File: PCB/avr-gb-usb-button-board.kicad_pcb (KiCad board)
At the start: 2 copper layers, 81 x 48 mm, 13 parts, among them IC1 ATTINY88-A

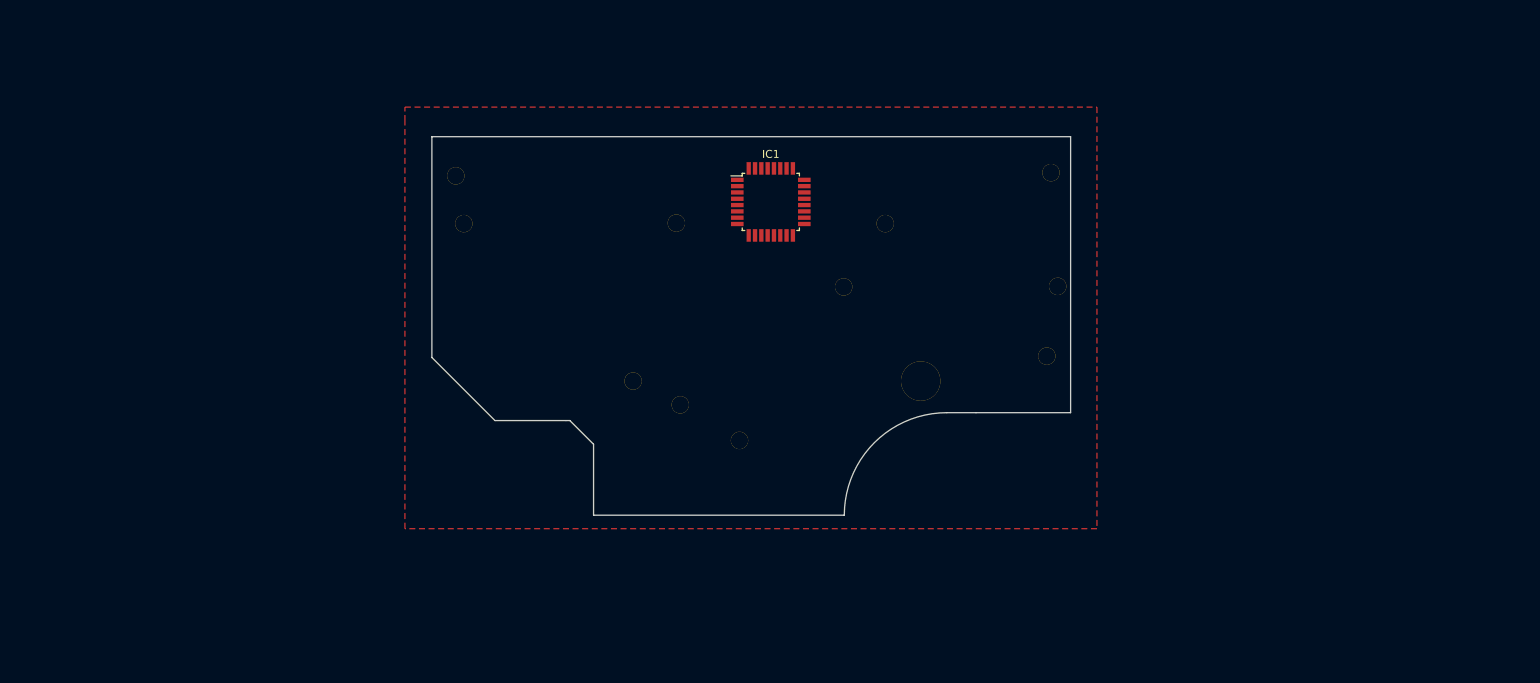
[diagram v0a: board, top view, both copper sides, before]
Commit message: Added mounting holes
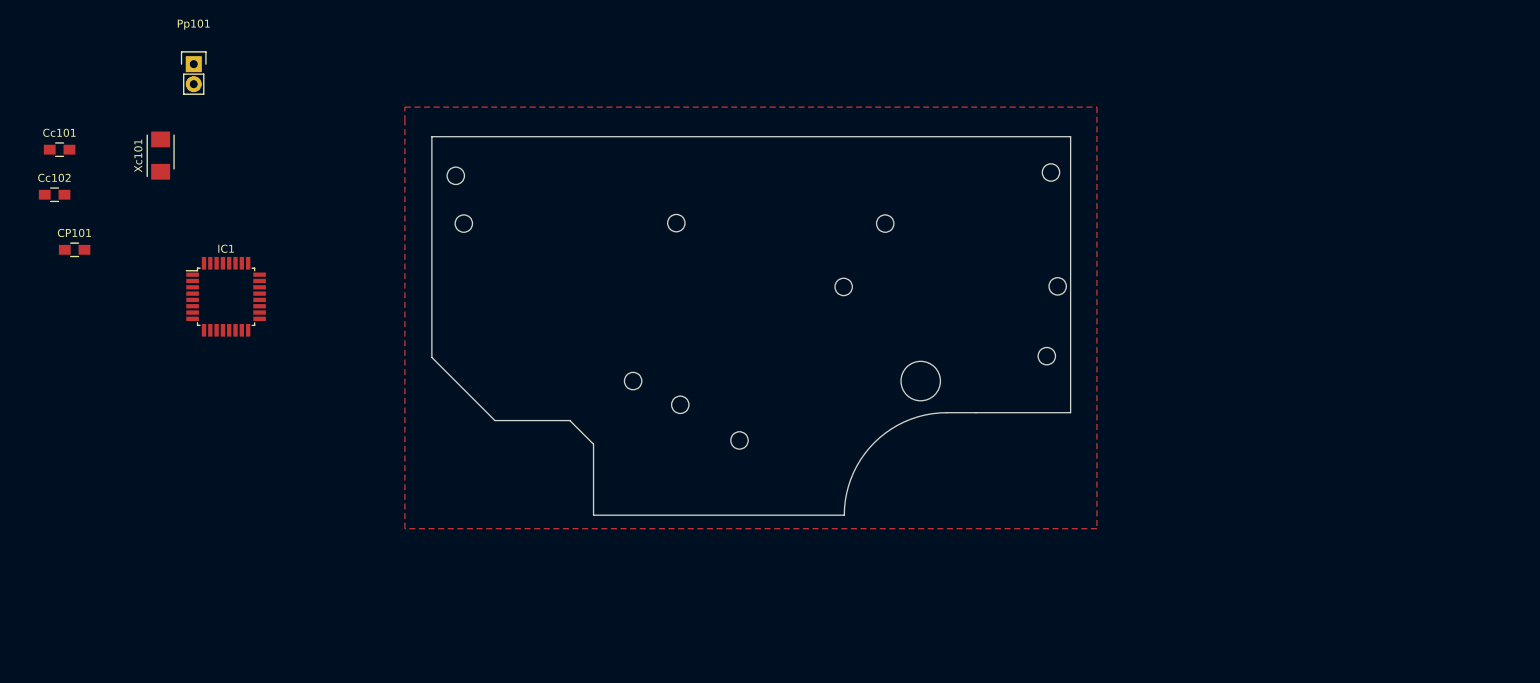
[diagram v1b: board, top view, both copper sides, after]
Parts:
- removed the ? at (44.9, 52.2)
- removed the ? at (50.4, 32.2)
- removed the ? at (23.4, 32.2)
- removed the ? at (22.4, 26.2)
- removed the ? at (50.9, 55.2)
- removed the ? at (58.4, 59.7)
- removed the ? at (81.4, 52.2)
- removed the ? at (97.4, 49.0)
- removed the ? at (98.8, 40.2)
- removed the ? at (97.9, 25.8)
- removed the ? at (76.9, 32.2)
- removed the ? at (71.6, 40.2)
- added ?: , Mounting_Holes:MountingHole_2.2mm_M2, F.Cu at (22.4, 26.2)
- added ?: , Mounting_Holes:MountingHole_2.2mm_M2, F.Cu at (50.9, 55.2)
- added ?: , Mounting_Holes:MountingHole_2.2mm_M2, F.Cu at (44.9, 52.2)
- added ?: , Mounting_Holes:MountingHole_5mm, F.Cu at (81.4, 52.2)
- added ?: , Mounting_Holes:MountingHole_2.2mm_M2, F.Cu at (23.4, 32.2)
- added ?: , Mounting_Holes:MountingHole_2.2mm_M2, F.Cu at (50.4, 32.2)
- added ?: , Mounting_Holes:MountingHole_2.2mm_M2, F.Cu at (76.9, 32.2)
- added ?: , Mounting_Holes:MountingHole_2.2mm_M2, F.Cu at (71.6, 40.2)
- added ?: , Mounting_Holes:MountingHole_2.2mm_M2, F.Cu at (97.9, 25.7)
- added ?: , Mounting_Holes:MountingHole_2.2mm_M2, F.Cu at (98.8, 40.2)
- added ?: , Mounting_Holes:MountingHole_2.2mm_M2, F.Cu at (97.4, 49.0)
- added ?: , Mounting_Holes:MountingHole_2.2mm_M2, F.Cu at (58.4, 59.7)
- added CP101: C, Capacitors_SMD:C_0805_HandSoldering, F.Cu at (-25.9, 35.5)
- added Cc101: 22pF, Capacitors_SMD:C_0805_HandSoldering, F.Cu at (-27.8, 22.8)
- added Cc102: 22pF, Capacitors_SMD:C_0805_HandSoldering, F.Cu at (-28.4, 28.6)
- added Pp101: CONN_01X02, Pin_Headers:Pin_Header_Straight_1x02, F.Cu at (-10.8, 12.0)
- added Xc101: 12MHz, Crystals:Crystal_SMD_5032_2Pads, F.Cu at (-15.0, 23.6)
- moved IC1 70.1 mm to (-6.70, 41.5)
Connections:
- IC1 pad 1: (no net) -> Net-(IC1-Pad1)
- IC1 pad 10: (no net) -> Net-(IC1-Pad10)
- IC1 pad 11: (no net) -> Net-(IC1-Pad11)
- IC1 pad 12: (no net) -> Net-(IC1-Pad12)
- IC1 pad 13: (no net) -> Net-(IC1-Pad13)
- IC1 pad 14: (no net) -> Net-(IC1-Pad14)
- IC1 pad 15: (no net) -> Net-(IC1-Pad15)
- IC1 pad 16: (no net) -> Net-(IC1-Pad16)
- IC1 pad 17: (no net) -> Net-(Cc101-Pad2)
- IC1 pad 18: (no net) -> Net-(IC1-Pad18)
- IC1 pad 19: (no net) -> Net-(IC1-Pad19)
- IC1 pad 2: (no net) -> Net-(IC1-Pad2)
- IC1 pad 20: (no net) -> Net-(IC1-Pad20)
- IC1 pad 21: (no net) -> Net-(IC1-Pad21)
- IC1 pad 22: (no net) -> Net-(IC1-Pad22)
- IC1 pad 23: (no net) -> Net-(IC1-Pad23)
- IC1 pad 24: (no net) -> Net-(IC1-Pad24)
- IC1 pad 25: (no net) -> Net-(IC1-Pad25)
- IC1 pad 26: (no net) -> Net-(IC1-Pad26)
- IC1 pad 27: (no net) -> Net-(IC1-Pad27)
- IC1 pad 28: (no net) -> Net-(IC1-Pad28)
- IC1 pad 29: (no net) -> Net-(IC1-Pad29)
- IC1 pad 3: (no net) -> Net-(IC1-Pad3)
- IC1 pad 30: (no net) -> Net-(IC1-Pad30)
- IC1 pad 31: (no net) -> Net-(IC1-Pad31)
- IC1 pad 32: (no net) -> Net-(IC1-Pad32)
- IC1 pad 4: (no net) -> VCC
- IC1 pad 6: (no net) -> Net-(IC1-Pad6)
- IC1 pad 7: (no net) -> Net-(Cc102-Pad2)
- IC1 pad 8: (no net) -> Net-(IC1-Pad8)
- IC1 pad 9: (no net) -> Net-(IC1-Pad9)

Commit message: Added ABXY button markers
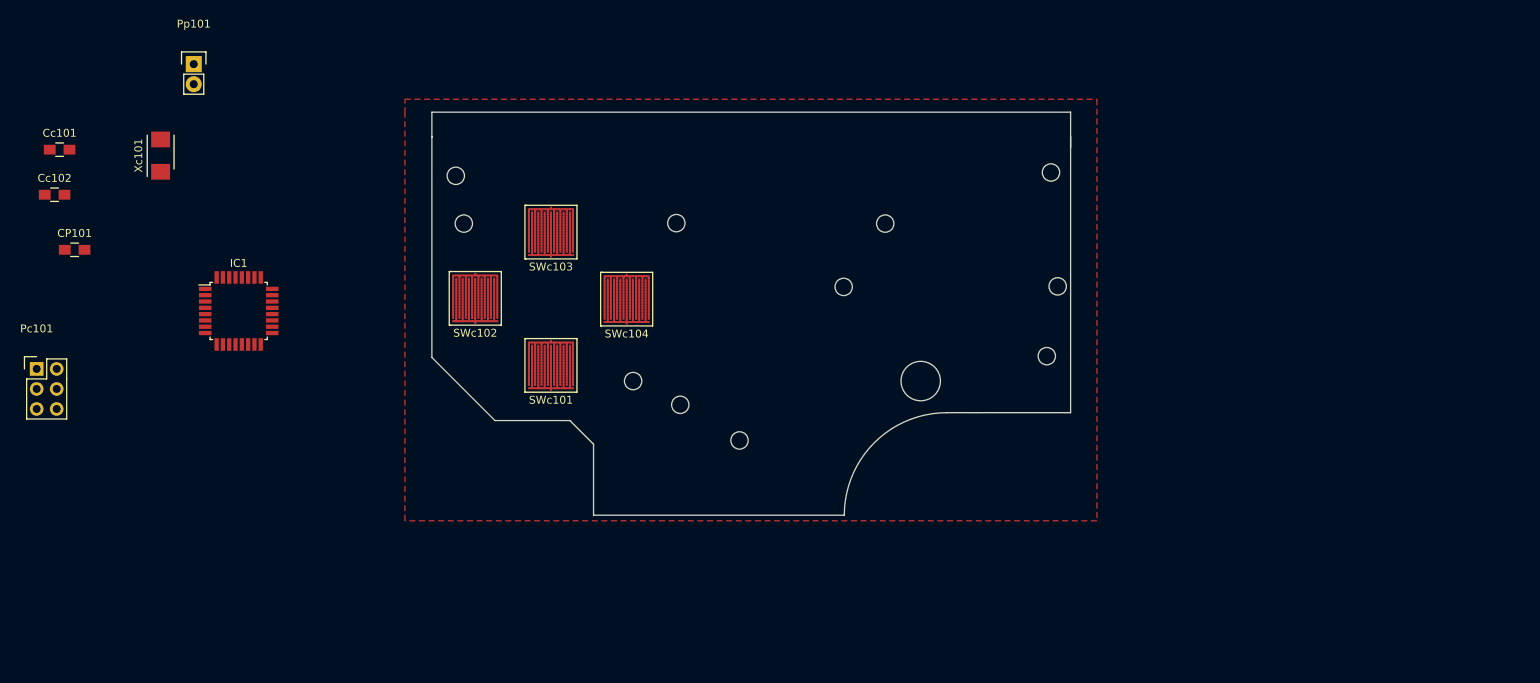
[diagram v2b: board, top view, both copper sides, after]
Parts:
- added Pc101: CONN_02X03, Pin_Headers:Pin_Header_Straight_2x03, F.Cu at (-30.7, 50.6)
- added SWc101: SW_PUSH, GBFootprints:GBButtonPad5mm, F.Cu at (34.5, 49.9)
- added SWc102: SW_PUSH, GBFootprints:GBButtonPad5mm, F.Cu at (24.9, 41.4)
- added SWc103: SW_PUSH, GBFootprints:GBButtonPad5mm, F.Cu at (34.5, 33.0)
- added SWc104: SW_PUSH, GBFootprints:GBButtonPad5mm, F.Cu at (44.1, 41.5)
- moved IC1 2.41 mm to (-5.10, 43.3)
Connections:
- IC1 pad 17: Net-(Cc101-Pad2) -> Net-(IC1-Pad17)
- IC1 pad 7: Net-(Cc102-Pad2) -> Net-(IC1-Pad7)
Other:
- board size 81 x 48 mm -> 81 x 51.1 mm

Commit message: Placed start and select buttons
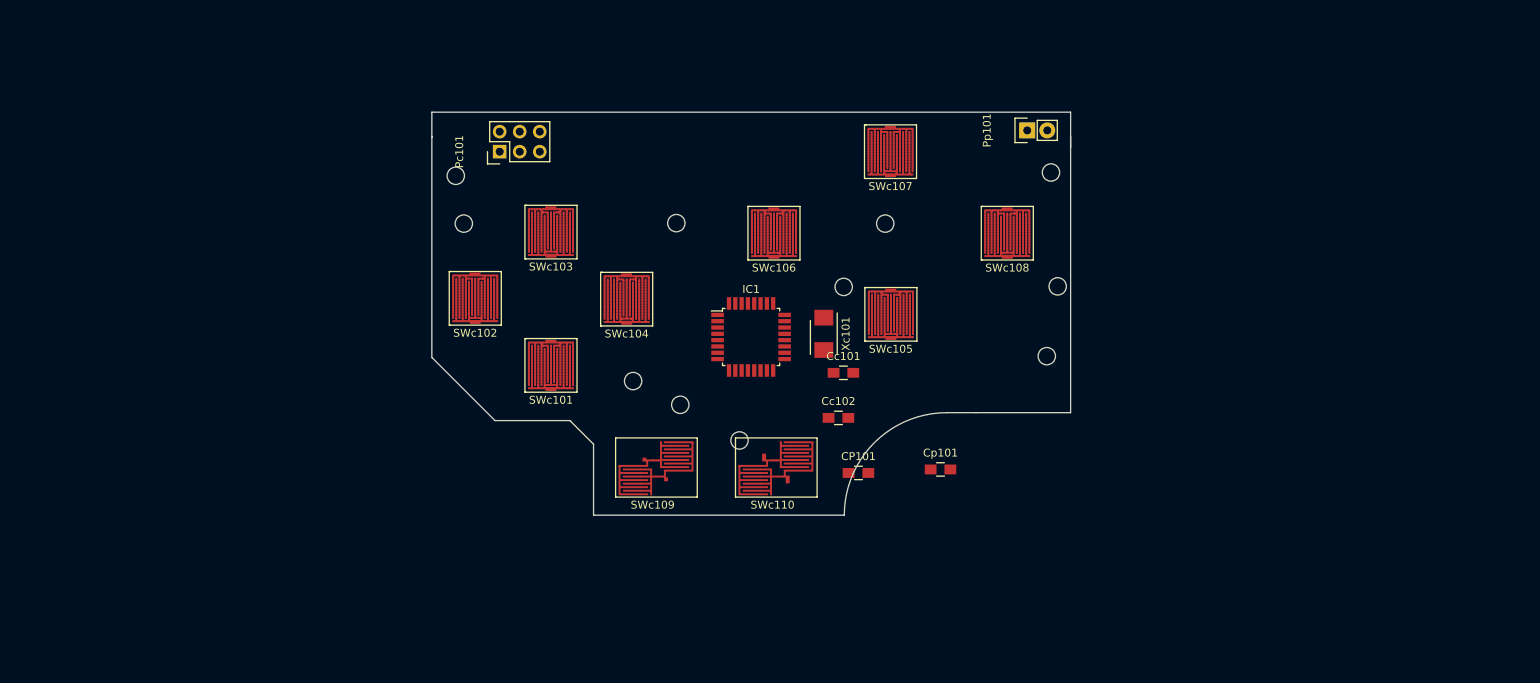
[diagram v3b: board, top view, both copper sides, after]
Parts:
- removed the ? at (81.4, 52.2)
- added Cp101: C, Capacitors_SMD:C_0805_HandSoldering, F.Cu at (83.9, 63.4)
- added SWc105: SW_PUSH, GBFootprints:GBButtonPad5mm, F.Cu at (77.6, 43.4)
- added SWc106: SW_PUSH, GBFootprints:GBButtonPad5mm, F.Cu at (62.8, 33.1)
- added SWc107: SW_PUSH, GBFootprints:GBButtonPad5mm, F.Cu at (77.6, 22.8)
- added SWc108: SW_PUSH, GBFootprints:GBButtonPad5mm, F.Cu at (92.4, 33.1)
- added SWc109: SW_PUSH, GBFootprints:GBButtonPad3mm, F.Cu at (47.4, 63.4)
- added SWc110: SW_PUSH, GBFootprints:GBButtonPad3mm, F.Cu at (62.6, 63.4)
- moved Pp101 106.0 mm to (94.9, 20.4), turned to 90 degrees
- moved CP101 103.4 mm to (73.5, 63.8)
- moved Cc101 103.4 mm to (71.6, 51.1)
- moved Cc102 103.4 mm to (71.0, 56.9)
- moved Xc101 87.1 mm to (69.1, 46.2), turned to 270 degrees
- moved IC1 65.1 mm to (59.9, 46.6)
- moved Pc101 64.9 mm to (28.0, 23.1), turned to 90 degrees
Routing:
- removed copper zone on F.Cu, net GND
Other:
- net class Button Connect added: clearance 0, trace_width 0.25, via_dia 0.6, via_drill 0.4

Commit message: Wired buttons
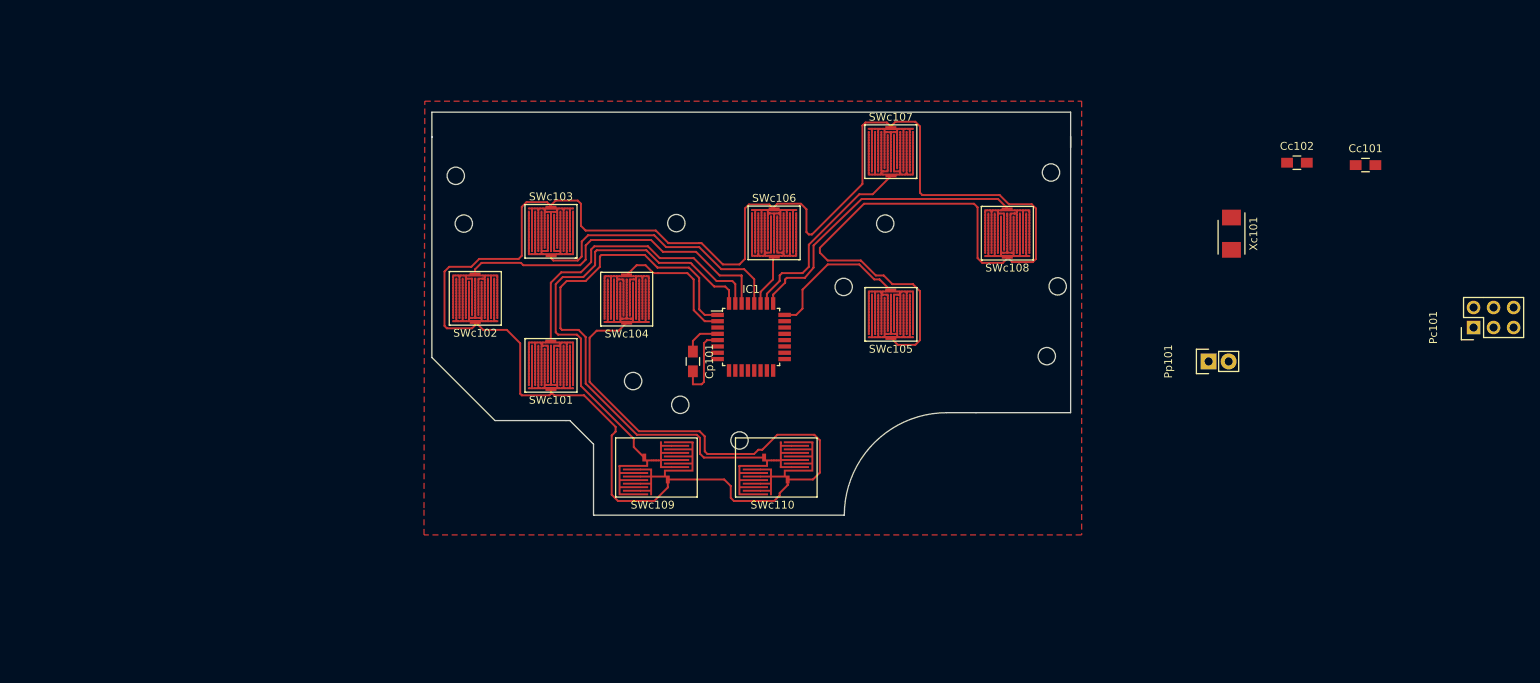
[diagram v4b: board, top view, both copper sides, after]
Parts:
- removed CP101: C, Capacitors_SMD:C_0805_HandSoldering
- Cp101: value C -> 10uF
- moved Pc101 125.5 mm to (151.5, 45.4)
- moved Cc101 71.3 mm to (137.8, 24.8)
- moved Cc102 66.5 mm to (129.1, 24.5)
- moved Xc101 53.2 mm to (120.8, 33.5)
- moved Pp101 37.2 mm to (117.9, 49.7)
- moved Cp101 34.3 mm to (52.5, 49.7), turned to 270 degrees
- moved SWc107 0.60 mm to (77.6, 23.4), turned to 180 degrees
- moved SWc106 0.56 mm to (62.8, 33.7), turned to 180 degrees
- moved SWc103 0.50 mm to (34.5, 33.5), turned to 180 degrees
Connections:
- SWc101 pad 1: Net-(IC1-Pad19) -> Net-(IC1-Pad31)
- SWc102 pad 1: Net-(IC1-Pad22) -> Net-(IC1-Pad30)
- SWc103 pad 1: Net-(IC1-Pad12) -> Net-(IC1-Pad28)
- SWc104 pad 1: Net-(IC1-Pad13) -> Net-(IC1-Pad2)
- SWc105 pad 1: Net-(IC1-Pad14) -> Net-(IC1-Pad24)
- SWc106 pad 1: Net-(IC1-Pad15) -> Net-(IC1-Pad27)
- SWc107 pad 1: Net-(IC1-Pad16) -> Net-(IC1-Pad26)
- SWc108 pad 1: Net-(IC1-Pad23) -> Net-(IC1-Pad25)
- SWc109 pad 1: Net-(IC1-Pad24) -> Net-(IC1-Pad32)
- SWc110 pad 1: Net-(IC1-Pad25) -> Net-(IC1-Pad1)
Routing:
- net GND: track 0.13 -> 331.2 mm
- net Net-(IC1-Pad1): track 0.00 -> 70.3 mm
- net Net-(IC1-Pad32): track 0.00 -> 56.6 mm
- net Net-(IC1-Pad30): track 0.00 -> 42.7 mm
- net Net-(IC1-Pad25): track 0.00 -> 38.3 mm
- net Net-(IC1-Pad31): track 0.00 -> 38.2 mm
- net Net-(IC1-Pad28): track 0.00 -> 34.1 mm
- net Net-(IC1-Pad26): track 0.00 -> 25.3 mm
- net Net-(IC1-Pad24): track 0.00 -> 18.9 mm
- net Net-(IC1-Pad2): track 0.00 -> 17.3 mm
- net Net-(IC1-Pad27): track 0.00 -> 6.65 mm
- net VCC: track 0.00 -> 4.85 mm
- added copper zone on F.Cu, net GND
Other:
- net class Button Connect removed

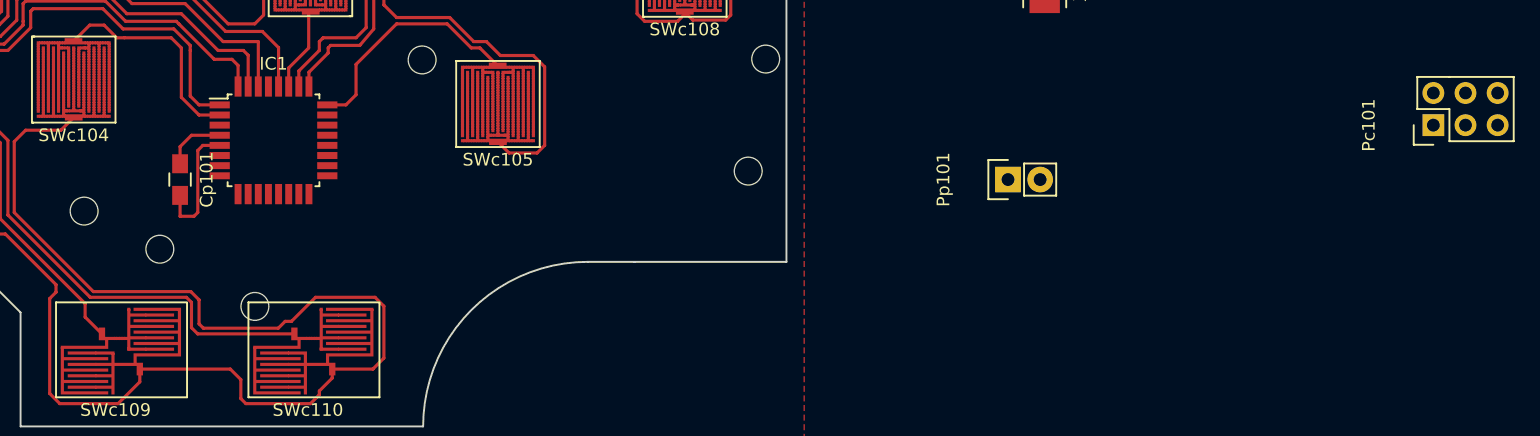
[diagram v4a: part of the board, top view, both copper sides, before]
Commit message: Connected VCC
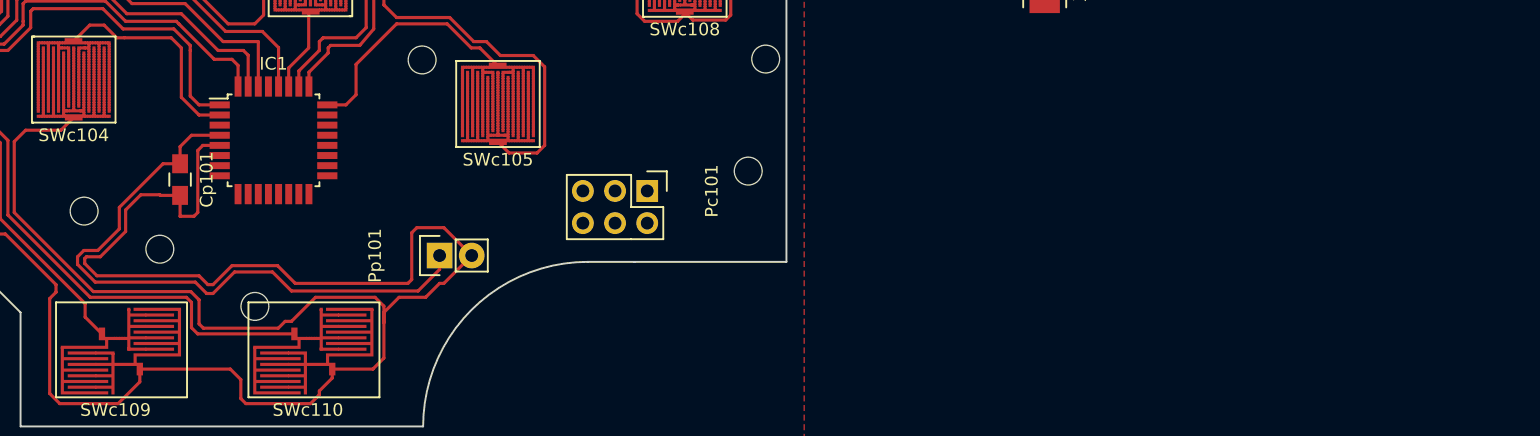
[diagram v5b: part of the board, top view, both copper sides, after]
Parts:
- moved Pc101 62.3 mm to (89.4, 50.6), turned to 270 degrees
- moved Pp101 45.3 mm to (73.0, 55.7)
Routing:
- net GND: track 331.2 -> 389.2 mm
- net VCC: track 4.85 -> 50.3 mm
